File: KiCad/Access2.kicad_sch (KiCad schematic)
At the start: 65 parts, among them J1 USB-C, J2 RFID, J3 INPUTS, J4 ExtTamper, J5 POWER, J6 DOOR, Q1 NX7002AK, SW1 Tamper, U1 ESP32-PICO-MINI-02, U2 FT231XQ, U3 G3VM-41GR8, U4 LMR16006+FB, U5 LMR16006+FB, U6 AA, U7 QR

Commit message: Start on new Bell2 board
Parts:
- U2: footprint RevK:QFN-20-1EP_4x4mm_P0.5mm_EP2.5x2.5mm -> Package_DFN_QFN:QFN-20-1EP_4x4mm_P0.5mm_EP2.5x2.5mm
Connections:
- no-connect marks 5 -> 15
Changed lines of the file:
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@@
   (no_connect (at 120.015 52.07))
   (no_connect (at 120.015 49.53))
+  (no_connect (at 30.48 50.8))
+  (no_connect (at 30.48 43.18))
+  (no_connect (at 30.48 45.72))
+  (no_connect (at 30.48 48.26))
+  (no_connect (at 60.96 76.2))
+  (no_connect (at 30.48 53.34))
+  (no_connect (at 30.48 55.88))
+  (no_connect (at 30.48 63.5))
+  (no_connect (at 30.48 68.58))
+  (no_connect (at 30.48 78.74))
   (wire (pts (xy 236.855 85.725) (xy 243.205 85.725))
     (stroke (width 0) (type default) (color 0 0 0 0))
@@
     (property "Reference" "U2" (id 0) (at 40.005 179.07 0))
     (property "Value" "FT231XQ" (id 1) (at 51.435 163.83 0))
-    (property "Footprint" "RevK:QFN-20-1EP_4x4mm_P0.5mm_EP2.5x2.5mm" (id 2) (at 87.63 177.8 0)
+    (property "Footprint" "Package_DFN_QFN:QFN-20-1EP_4x4mm_P0.5mm_EP2.5x2.5mm" (id 2) (at 87.63 177.8 0)
       (effects (font (size 1.27 1.27)) hide)
     )
@@
     (pin "1")
   )
-  (symbol (lib_name "Hidden_3") (lib_id "RevK:Hidden") (at 259.08 86.36 0) (unit 1)
+  (symbol (lib_id "RevK:Hidden") (at 259.08 86.36 0) (unit 1)
     (in_bom yes) (on_board yes)
     (property "Reference" "C9" (id 0) (at 259.715 86.36 0)
@@
     (pin "~")
   )
-  (symbol (lib_name "Hidden_4") (lib_id "RevK:Hidden") (at 259.08 88.265 0) (unit 1)
+  (symbol (lib_id "RevK:Hidden") (at 259.08 88.265 0) (unit 1)
     (in_bom yes) (on_board yes)
     (property "Reference" "C10" (id 0) (at 259.715 88.265 0)
@@
     (pin "~")
   )
-  (symbol (lib_name "Hidden_1") (lib_id "RevK:Hidden") (at 259.08 90.17 0) (unit 1)
+  (symbol (lib_id "RevK:Hidden") (at 259.08 90.17 0) (unit 1)
     (in_bom yes) (on_board yes)
     (property "Reference" "C11" (id 0) (at 259.715 90.17 0)
@@
     (pin "~")
   )
-  (symbol (lib_name "Hidden_2") (lib_id "RevK:Hidden") (at 259.08 92.075 0) (unit 1)
+  (symbol (lib_id "RevK:Hidden") (at 259.08 92.075 0) (unit 1)
     (in_bom yes) (on_board yes)
     (property "Reference" "L1" (id 0) (at 259.715 92.075 0)
@@
     (pin "~")
   )
-  (symbol (lib_name "Hidden_5") (lib_id "RevK:Hidden") (at 259.08 93.98 0) (unit 1)
+  (symbol (lib_id "RevK:Hidden") (at 259.08 93.98 0) (unit 1)
     (in_bom yes) (on_board yes)
     (property "Reference" "D6" (id 0) (at 259.715 93.98 0)
@@
     (pin "~")
   )
-  (symbol (lib_name "Hidden_7") (lib_id "RevK:Hidden") (at 259.715 118.11 0) (unit 1)
+  (symbol (lib_id "RevK:Hidden") (at 259.715 118.11 0) (unit 1)
     (in_bom yes) (on_board yes)
     (property "Reference" "C12" (id 0) (at 260.35 118.11 0)
@@
     (pin "~")
   )
-  (symbol (lib_name "Hidden_8") (lib_id "RevK:Hidden") (at 259.715 120.015 0) (unit 1)
+  (symbol (lib_id "RevK:Hidden") (at 259.715 120.015 0) (unit 1)
     (in_bom yes) (on_board yes)
     (property "Reference" "C13" (id 0) (at 260.35 120.015 0)
@@
     (pin "~")
   )
-  (symbol (lib_name "Hidden_6") (lib_id "RevK:Hidden") (at 259.715 121.92 0) (unit 1)
+  (symbol (lib_id "RevK:Hidden") (at 259.715 121.92 0) (unit 1)
     (in_bom yes) (on_board yes)
     (property "Reference" "C14" (id 0) (at 260.35 121.92 0)
@@
     (pin "~")
   )
-  (symbol (lib_name "Hidden_9") (lib_id "RevK:Hidden") (at 259.715 123.825 0) (unit 1)
+  (symbol (lib_id "RevK:Hidden") (at 259.715 123.825 0) (unit 1)
     (in_bom yes) (on_board yes)
     (property "Reference" "L2" (id 0) (at 260.35 123.825 0)
@@
     (pin "~")
   )
-  (symbol (lib_name "Hidden_10") (lib_id "RevK:Hidden") (at 259.715 125.73 0) (unit 1)
+  (symbol (lib_id "RevK:Hidden") (at 259.715 125.73 0) (unit 1)
     (in_bom yes) (on_board yes)
     (property "Reference" "D7" (id 0) (at 260.35 125.73 0)
@@
     )
     (path "/00000000-0000-0000-0000-00006084108b"
-      (reference "U2") (unit 1) (value "FT231XQ") (footprint "RevK:QFN-20-1EP_4x4mm_P0.5mm_EP2.5x2.5mm")
+      (reference "U2") (unit 1) (value "FT231XQ") (footprint "Package_DFN_QFN:QFN-20-1EP_4x4mm_P0.5mm_EP2.5x2.5mm")
     )
     (path "/00000000-0000-0000-0000-0000608bf21e"

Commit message: Started Keypad2 - may scrap it though.
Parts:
- R17: value 732R -> 680R
- R19: value 324R -> 220R
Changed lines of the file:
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@@
     (in_bom yes) (on_board yes)
     (property "Reference" "R19" (id 0) (at 177.165 88.265 90))
-    (property "Value" "324R" (id 1) (at 177.165 86.36 90))
+    (property "Value" "220R" (id 1) (at 177.165 86.36 90))
     (property "Footprint" "RevK:R_0603" (id 2) (at 177.165 84.582 90)
       (effects (font (size 1.27 1.27)) hide)
@@
     (in_bom yes) (on_board yes)
     (property "Reference" "R17" (id 0) (at 177.165 78.105 90))
-    (property "Value" "732R" (id 1) (at 177.165 76.2 90))
+    (property "Value" "680R" (id 1) (at 177.165 76.2 90))
     (property "Footprint" "RevK:R_0603" (id 2) (at 177.165 74.422 90)
       (effects (font (size 1.27 1.27)) hide)
@@
     )
     (path "/00000000-0000-0000-0000-000060cf9e4d"
-      (reference "R17") (unit 1) (value "732R") (footprint "RevK:R_0603")
+      (reference "R17") (unit 1) (value "680R") (footprint "RevK:R_0603")
     )
     (path "/00000000-0000-0000-0000-000060cfbfaf"
@@
     )
     (path "/00000000-0000-0000-0000-000060a436c8"
-      (reference "R19") (unit 1) (value "324R") (footprint "RevK:R_0603")
+      (reference "R19") (unit 1) (value "220R") (footprint "RevK:R_0603")
     )
     (path "/00000000-0000-0000-0000-0000609872b4"

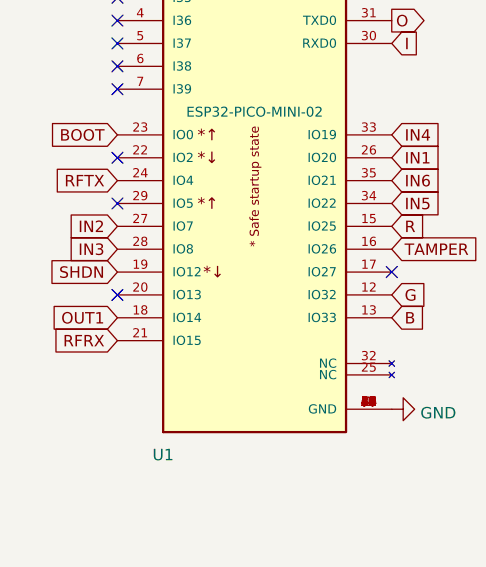
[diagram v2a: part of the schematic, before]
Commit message: Tweaked some GPIO, and added to documentation
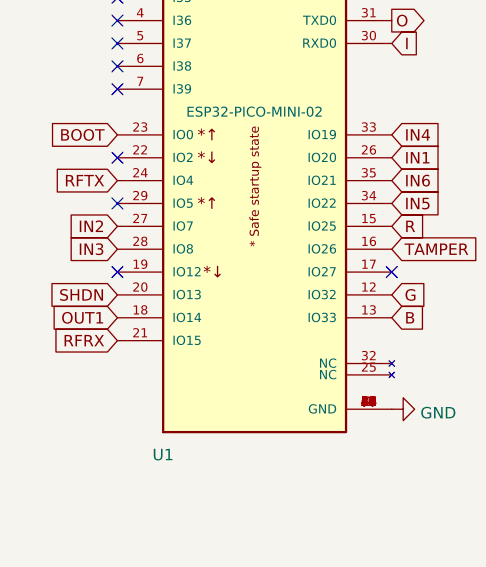
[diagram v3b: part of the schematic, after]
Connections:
- net SHDN: now also U1.20 (IO13); no longer U1.19 (IO12)
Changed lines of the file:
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@@
   (no_connect (at 30.48 63.5))
   (no_connect (at 30.48 68.58))
-  (no_connect (at 30.48 78.74))
+  (no_connect (at 30.48 76.2))
   (wire (pts (xy 236.855 85.725) (xy 243.205 85.725))
     (stroke (width 0) (type default) (color 0 0 0 0))
@@
     )
   )
-  (global_label "SHDN" (shape input) (at 30.48 76.2 180) (fields_autoplaced)
-    (effects (font (size 1.27 1.27)) (justify right))
-    (property "Intersheet References" "${INTERSHEET_REFS}" (id 0) (at 92.71 118.745 0)
-      (effects (font (size 1.27 1.27)) hide)
-    )
+  (global_label "SHDN" (shape input) (at 30.48 78.74 180) (fields_autoplaced)
+    (effects (font (size 1.27 1.27)) (justify right))
+    (property "Intersheet References" "${INTERSHEET_REFS}" (id 0) (at 92.71 121.285 0)
+      (effects (font (size 1.27 1.27)) hide)
+    )

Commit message: Tidy
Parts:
- removed U2: FT231XQ, Package_DFN_QFN:QFN-20-1EP_4x4mm_P0.5mm_EP2.5x2.5mm, symbol Interface_USB:FT231XQ
- added U2: FT231XQ, RevK:QFN-20-1EP_4x4mm_P0.5mm_EP2.5x2.5mm, symbol RevK:FT231XQ
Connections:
- net +3V3: now also U2.10 (3V3OUT), U2.11 (~{RESET}), U2.12 (VCC), U2.20 (VCCIO)
- net BOOT: now also U2.18 (~{DTR})
- net D+: now also U2.8 (USBDP)
- net D-: now also U2.9 (USBDM)
- net EN: now also U2.19 (~{RTS})
- net GND: now also U2.13 (GND), U2.2 (~{RI}), U2.21 (GND), U2.3 (GND), U2.4 (~{DSR}), U2.5 (~{DCD}), U2.6 (~{CTS})
- net I: now also U2.17 (TXD)
- net O: now also U2.1 (RXD)
- net at R2.2, R3.1: now also U2.7 (CBUS2)

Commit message: Clean up
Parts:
- J1: symbol Connector:USB_C_Receptacle_USB2.0 -> RevK:USB-C
- SW1: now left out of the parts list
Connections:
- net GND: no longer U1.54 (GND), U1.55 (GND), U1.56 (GND), U1.57 (GND), U1.58 (GND), U1.59 (GND), U1.60 (GND), U1.61 (GND)
- no-connect marks 15 -> 13
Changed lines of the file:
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@@
   (no_connect (at 71.12 165.1))
   (no_connect (at 71.12 172.72))
-  (no_connect (at 120.015 52.07))
-  (no_connect (at 120.015 49.53))
   (no_connect (at 30.48 50.8))
   (no_connect (at 30.48 43.18))
@@
     )
   )
-  (symbol (lib_id "Connector:USB_C_Receptacle_USB2.0") (at 104.775 36.83 0) (unit 1)
+  (symbol (lib_id "RevK:USB-C") (at 104.775 36.83 0) (unit 1)
     (in_bom yes) (on_board yes)
     (property "Reference" "J1" (id 0) (at 107.4928 14.8082 0))
@@
   (symbol (lib_id "RevK:PowerIn") (at 207.01 22.86 0) (unit 1)
     (in_bom yes) (on_board yes)
-    (property "Reference" "J5" (id 0) (at 209.042 23.0632 0)
-      (effects (font (size 1.27 1.27)) (justify left))
-    )
-    (property "Value" "POWER" (id 1) (at 209.042 25.3746 0)
+    (property "Reference" "J5" (id 0) (at 208.28 27.94 0)
+      (effects (font (size 1.27 1.27)) (justify left))
+    )
+    (property "Value" "POWER" (id 1) (at 205.74 20.32 0)
       (effects (font (size 1.27 1.27)) (justify left))
     )
@@
   )
   (symbol (lib_id "Switch:SW_Push") (at 183.515 111.76 0) (unit 1)
-    (in_bom yes) (on_board yes)
+    (in_bom no) (on_board yes)
     (property "Reference" "SW1" (id 0) (at 183.515 104.521 0))
     (property "Value" "Tamper" (id 1) (at 183.515 106.8324 0))
@@
     (pin "52")
     (pin "53")
-    (pin "54")
-    (pin "55")
-    (pin "56")
-    (pin "57")
-    (pin "58")
-    (pin "59")
     (pin "6")
-    (pin "60")
-    (pin "61")
     (pin "7")
     (pin "8")

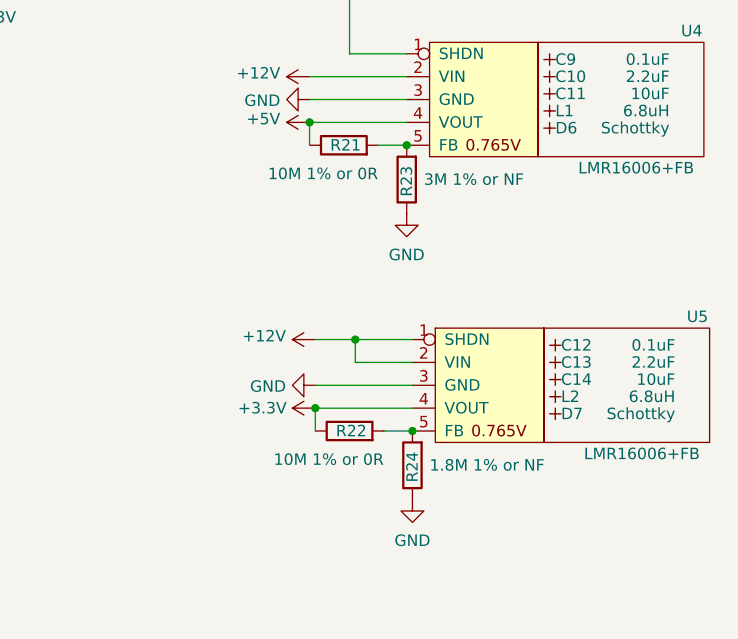
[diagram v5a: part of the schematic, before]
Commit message: Resistor fixes
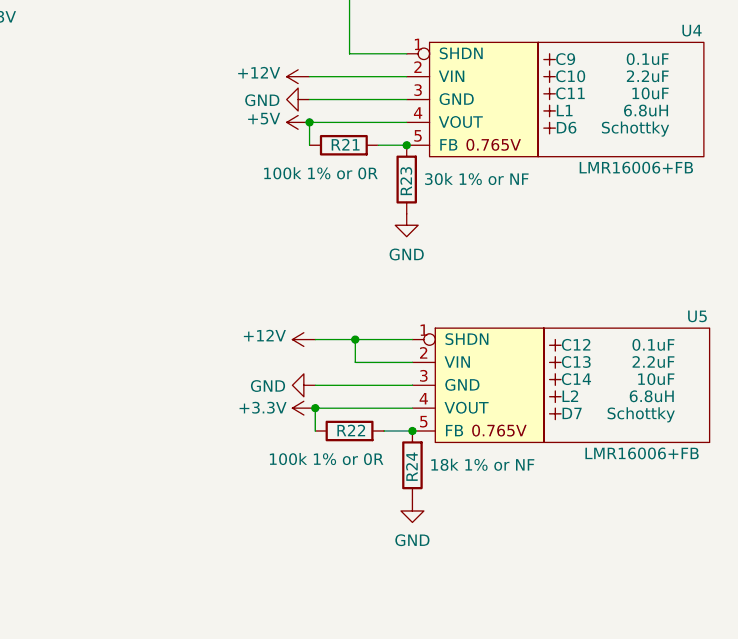
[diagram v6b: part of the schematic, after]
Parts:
- R21, R22: value 10M 1% or 0R -> 100k 1% or 0R
- R23: value 3M 1% or NF -> 30k 1% or NF
- R24: value 1.8M 1% or NF -> 18k 1% or NF
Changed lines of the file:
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@@
       (effects (font (size 1.27 1.27)) (justify left))
     )
-    (property "Value" "10M 1% or 0R" (id 1) (at 240.03 99.06 90)
+    (property "Value" "100k 1% or 0R" (id 1) (at 240.03 99.06 90)
       (effects (font (size 1.27 1.27)) (justify left))
     )
@@
       (effects (font (size 1.27 1.27)) (justify left))
     )
-    (property "Value" "10M 1% or 0R" (id 1) (at 240.665 130.81 90)
+    (property "Value" "100k 1% or 0R" (id 1) (at 240.665 130.81 90)
       (effects (font (size 1.27 1.27)) (justify left))
     )
@@
       (effects (font (size 1.27 1.27)) (justify right))
     )
-    (property "Value" "1.8M 1% or NF" (id 1) (at 245.745 131.445 0)
+    (property "Value" "18k 1% or NF" (id 1) (at 245.745 131.445 0)
       (effects (font (size 1.27 1.27)) (justify right))
     )
@@
       (effects (font (size 1.27 1.27)) (justify right))
     )
-    (property "Value" "3M 1% or NF" (id 1) (at 245.11 99.695 0)
+    (property "Value" "30k 1% or NF" (id 1) (at 245.11 99.695 0)
       (effects (font (size 1.27 1.27)) (justify right))
     )
@@
     )
     (path "/0a7f75d0-9f86-4caa-a0e4-44ff4b8f6861"
-      (reference "R21") (unit 1) (value "10M 1% or 0R") (footprint "RevK:R_0603")
+      (reference "R21") (unit 1) (value "100k 1% or 0R") (footprint "RevK:R_0603")
     )
     (path "/0d353d81-a7d7-4ff0-89eb-60271d9c4a01"
-      (reference "R22") (unit 1) (value "10M 1% or 0R") (footprint "RevK:R_0603")
+      (reference "R22") (unit 1) (value "100k 1% or 0R") (footprint "RevK:R_0603")
     )
     (path "/d571cde4-c062-4e90-8e0a-c6147d1b6cd4"
-      (reference "R23") (unit 1) (value "3M 1% or NF") (footprint "RevK:R_0603")
+      (reference "R23") (unit 1) (value "30k 1% or NF") (footprint "RevK:R_0603")
     )
     (path "/8271dfba-3962-4c80-a371-fd4d42efa2fe"
-      (reference "R24") (unit 1) (value "1.8M 1% or NF") (footprint "RevK:R_0603")
+      (reference "R24") (unit 1) (value "18k 1% or NF") (footprint "RevK:R_0603")
     )
     (path "/00000000-0000-0000-0000-00006093be97"

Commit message: Fix voltages
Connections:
- net at R22.2, U5.5 (FB): now also R23.2; no longer R24.2
- net at R21.2, U4.5 (FB): now also R24.2; no longer R23.2
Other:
- moved on the sheet: C10, C11, C12, C13, C14, C9, D6, D7, L1, L2, R21, R22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

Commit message: Library update
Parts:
- D8: footprint Diode_SMD:D_1206_3216Metric_Pad1.42x1.75mm_HandSolder -> RevK:D_1206
- U7: now left out of the parts list
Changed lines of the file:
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@@
     (property "Reference" "D8" (id 0) (at 260.35 31.9532 0))
     (property "Value" "D" (id 1) (at 260.35 34.2646 0))
-    (property "Footprint" "Diode_SMD:D_1206_3216Metric_Pad1.42x1.75mm_HandSolder" (id 2) (at 260.35 37.465 0)
+    (property "Footprint" "RevK:D_1206" (id 2) (at 260.35 37.465 0)
       (effects (font (size 1.27 1.27)) hide)
     )
@@
   )
   (symbol (lib_id "RevK:QR") (at 273.05 174.625 0) (unit 1)
-    (in_bom yes) (on_board yes)
+    (in_bom no) (on_board yes)
     (property "Reference" "U7" (id 0) (at 273.05 177.8 0)
       (effects (font (size 1.27 1.27)) hide)
@@
     )
     (path "/00000000-0000-0000-0000-0000608d7f70"
-      (reference "D8") (unit 1) (value "D") (footprint "Diode_SMD:D_1206_3216Metric_Pad1.42x1.75mm_HandSolder")
+      (reference "D8") (unit 1) (value "D") (footprint "RevK:D_1206")
     )
     (path "/00000000-0000-0000-0000-000060436927"
